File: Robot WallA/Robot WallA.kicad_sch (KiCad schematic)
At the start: 4 parts

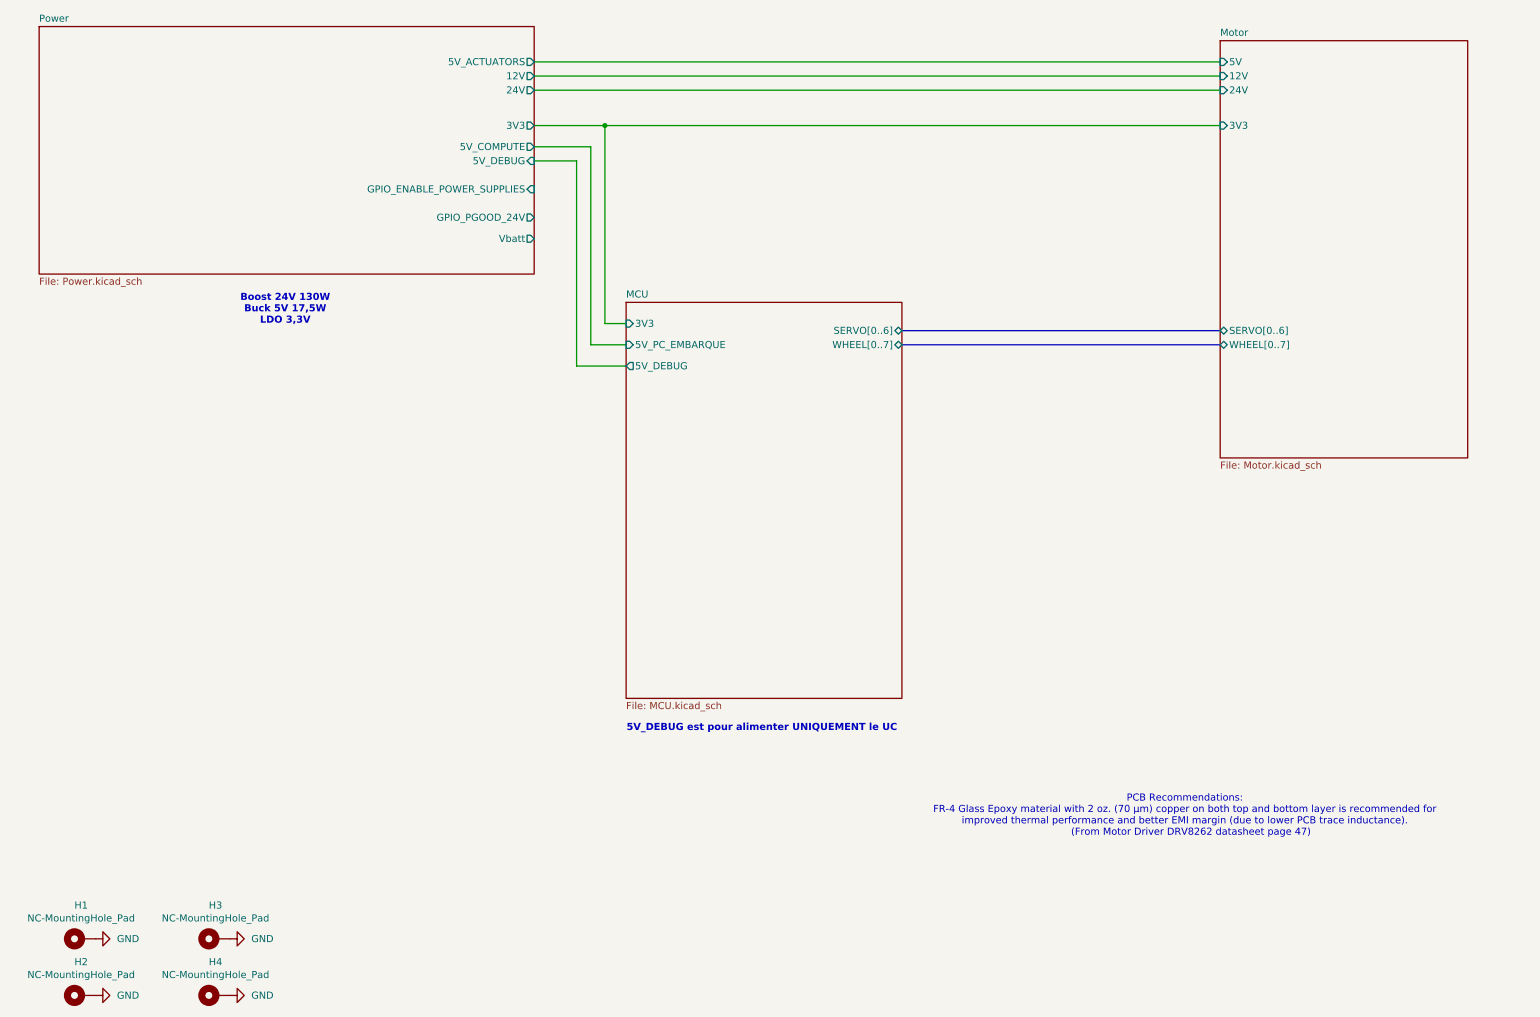
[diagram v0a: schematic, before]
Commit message: Continued to link MCU pins, Added a sheet for servomotors and optional 2 DC motors.
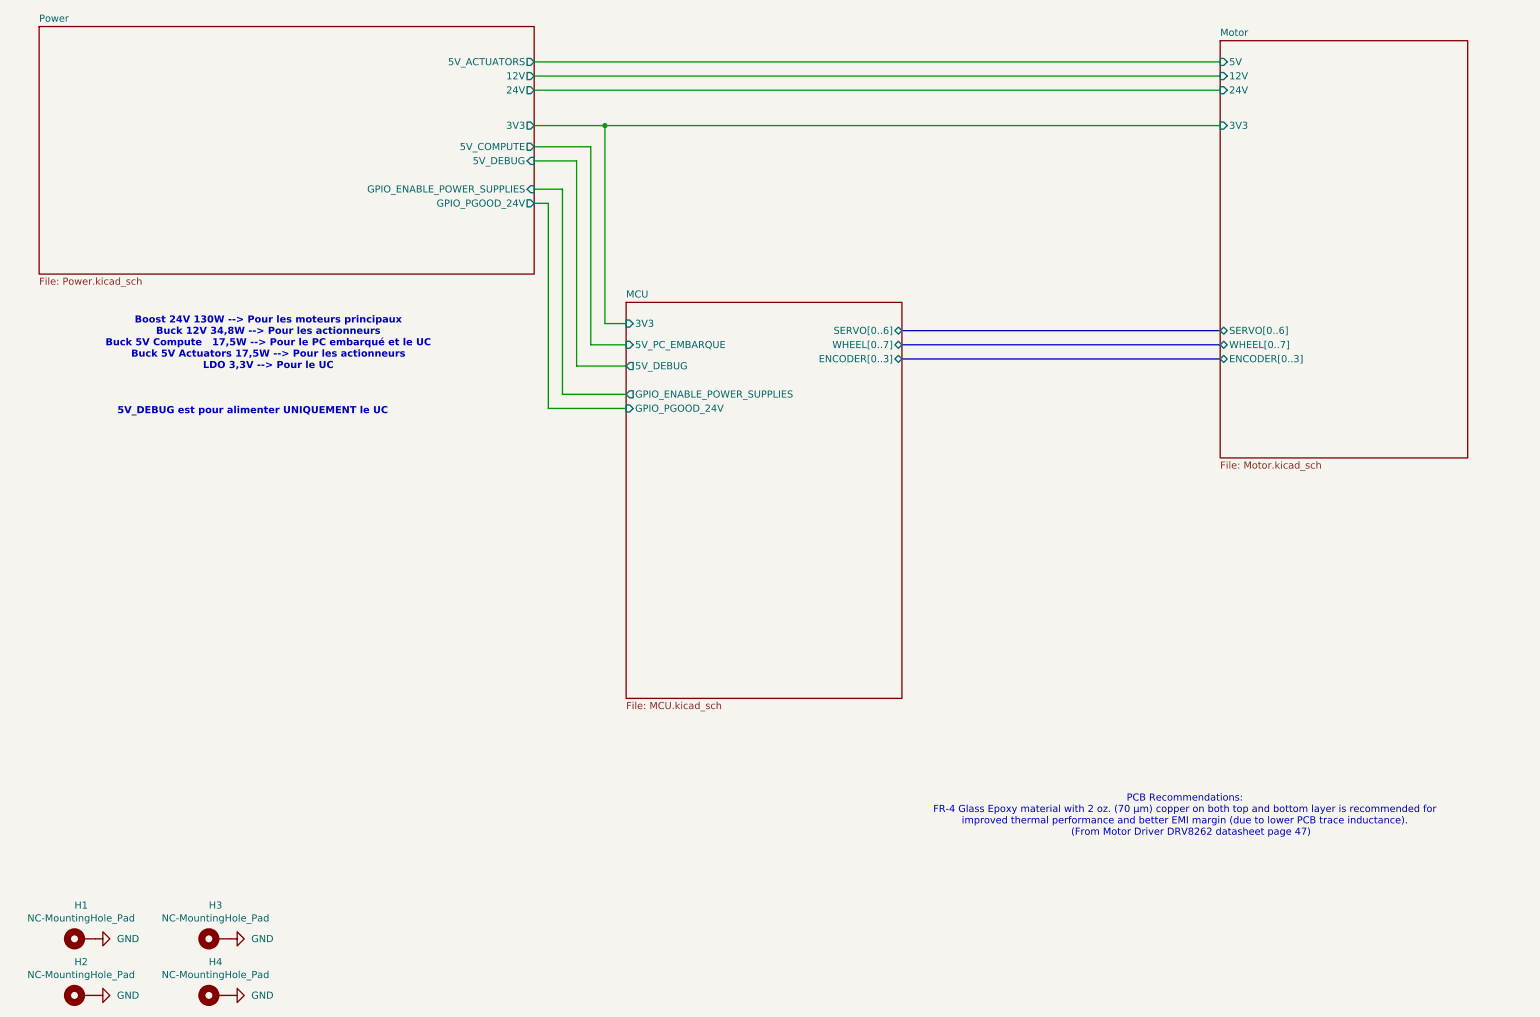
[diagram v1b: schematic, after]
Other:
- sheet MCU ports: added ENCODER[0..3], GPIO_ENABLE_POWER_SUPPLIES, GPIO_PGOOD_24V; removed none
- sheet Motor ports: added ENCODER[0..3]; removed none
- sheet Power ports: added none; removed Vbatt
- note added: "Boost 24V 130W --> Pour les moteurs principaux Buck 12V 34,8W --> Pour les actionneurs Buck 5V Compute 17,5W --> Pour le PC embarqué et le UC Buck 5V Actuators 17,5W --> Pour les actionneurs LDO 3,3V --> Pour le UC"
- note removed: "Boost 24V 130W Buck 5V 17,5W LDO 3,3V"
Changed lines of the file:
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@@
 	(text "5V_DEBUG est pour alimenter UNIQUEMENT le UC"
 		(exclude_from_sim no)
-		(at 150.114 142.494 0)
+		(at 58.674 85.598 0)
 		(effects
 			(font
@@
 		)
 	)
-	(text "Boost 24V 130W\nBuck 5V 17,5W\nLDO 3,3V"
-		(exclude_from_sim no)
-		(at 64.516 67.31 0)
+	(text "Boost 24V 130W --> Pour les moteurs principaux\nBuck 12V 34,8W --> Pour les actionneurs\nBuck 5V Compute   17,5W --> Pour le PC embarqué et le UC\nBuck 5V Actuators 17,5W --> Pour les actionneurs\nLDO 3,3V --> Pour le UC"
+		(exclude_from_sim no)
+		(at 61.468 73.406 0)
 		(effects
 			(font
@@
 	(wire
 		(pts
+			(xy 114.3 82.55) (xy 114.3 45.72)
+		)
+		(stroke
+			(width 0)
+			(type default)
+		)
+	)
+	(wire
+		(pts
 			(xy 109.22 27.94) (xy 232.41 27.94)
 		)
@@
 		)
 	)
+	(bus
+		(pts
+			(xy 175.26 76.2) (xy 232.41 76.2)
+		)
+		(stroke
+			(width 0)
+			(type default)
+		)
+	)
 	(wire
 		(pts
@@
 		)
 	)
+	(wire
+		(pts
+			(xy 109.22 48.26) (xy 111.76 48.26)
+		)
+		(stroke
+			(width 0)
+			(type default)
+		)
+	)
+	(wire
+		(pts
+			(xy 125.73 82.55) (xy 114.3 82.55)
+		)
+		(stroke
+			(width 0)
+			(type default)
+		)
+	)
 	(bus
 		(pts
@@
 	(wire
 		(pts
+			(xy 111.76 85.09) (xy 125.73 85.09)
+		)
+		(stroke
+			(width 0)
+			(type default)
+		)
+	)
+	(wire
+		(pts
 			(xy 119.38 73.66) (xy 125.73 73.66)
 		)
@@
 	(wire
 		(pts
+			(xy 111.76 48.26) (xy 111.76 85.09)
+		)
+		(stroke
+			(width 0)
+			(type default)
+		)
+	)
+	(wire
+		(pts
 			(xy 125.73 77.47) (xy 116.84 77.47)
 		)
@@
 		(pts
 			(xy 109.22 22.86) (xy 232.41 22.86)
+		)
+		(stroke
+			(width 0)
+			(type default)
+		)
+	)
+	(wire
+		(pts
+			(xy 114.3 45.72) (xy 109.22 45.72)
 		)
 		(stroke
@@
 		(dnp no)
 		(fields_autoplaced yes)
-		(property "Reference" "#PWR0113"
+		(property "Reference" "#PWR04"
 			(at 60.96 190.5 0)
 			(effects
@@
 			(project "PCB"
 				(path "/117fd49e-499d-4b54-b58c-f6b538ecca4a"
-					(reference "#PWR0113")
+					(reference "#PWR04")
 					(unit 1)
 				)
@@
 		(dnp no)
 		(fields_autoplaced yes)
-		(property "Reference" "#PWR0112"
+		(property "Reference" "#PWR03"
 			(at 60.96 180.34 0)
 			(effects
@@
 			(project "PCB"
 				(path "/117fd49e-499d-4b54-b58c-f6b538ecca4a"
-					(reference "#PWR0112")
+					(reference "#PWR03")
 					(unit 1)
 				)
@@
 		(dnp no)
 		(fields_autoplaced yes)
-		(property "Reference" "#PWR0110"
+		(property "Reference" "#PWR01"
 			(at 36.83 180.34 0)
 			(effects
@@
 			(project ""
 				(path "/117fd49e-499d-4b54-b58c-f6b538ecca4a"
-					(reference "#PWR0110")
+					(reference "#PWR01")
 					(unit 1)
 				)
@@
 		(dnp no)
 		(fields_autoplaced yes)
-		(property "Reference" "#PWR0111"
+		(property "Reference" "#PWR02"
 			(at 36.83 190.5 0)
 			(effects
@@
 			(project "PCB"
 				(path "/117fd49e-499d-4b54-b58c-f6b538ecca4a"
-					(reference "#PWR0111")
+					(reference "#PWR02")
 					(unit 1)
 				)
@@
 			)
 		)
+		(pin "ENCODER[0..3]" bidirectional
+			(at 232.41 76.2 180)
+			(effects
+				(font
+					(size 1.27 1.27)
+				)
+				(justify left)
+			)
+		)
 		(instances
-			(project "PCB"
+			(project "Robot WallA"
 				(path "/117fd49e-499d-4b54-b58c-f6b538ecca4a"
 					(page "3")
@@
 			)
 		)
+		(pin "ENCODER[0..3]" bidirectional
+			(at 175.26 76.2 0)
+			(effects
+				(font
+					(size 1.27 1.27)
+				)
+				(justify right)
+			)
+		)
+		(pin "GPIO_ENABLE_POWER_SUPPLIES" output
+			(at 125.73 82.55 180)
+			(effects
+				(font
+					(size 1.27 1.27)
+				)
+				(justify left)
+			)
+		)
+		(pin "GPIO_PGOOD_24V" input
+			(at 125.73 85.09 180)
+			(effects
+				(font
+					(size 1.27 1.27)
+				)
+				(justify left)
+			)
+		)
 		(instances
-			(project "PCB"
+			(project "Robot WallA"
 				(path "/117fd49e-499d-4b54-b58c-f6b538ecca4a"
 					(page "2")
@@
 		)
 		(pin "GPIO_PGOOD_24V" output
-			(at 109.22 50.8 0)
-			(effects
-				(font
-					(size 1.27 1.27)
-				)
-				(justify right)
-			)
-		)
-		(pin "Vbatt" output
-			(at 109.22 54.61 0)
+			(at 109.22 48.26 0)
 			(effects
 				(font
@@
 		)
 		(instances
-			(project "PCB"
+			(project "Robot WallA"
 				(path "/117fd49e-499d-4b54-b58c-f6b538ecca4a"
 					(page "5")

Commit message: Defined every footprints
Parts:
- H1, H4: value NC-MountingHole_Pad -> MountingHole_Pad; Manufacturer_Part_Number NC -> (none); Mouser Reference NC -> (none); RS Reference NC -> (none)
- H2: renamed from H3; value NC-MountingHole_Pad -> MountingHole_Pad; Manufacturer_Part_Number NC -> (none); Mouser Reference NC -> (none); RS Reference NC -> (none)
- H3: renamed from H2; value NC-MountingHole_Pad -> MountingHole_Pad; Manufacturer_Part_Number NC -> (none); Mouser Reference NC -> (none); RS Reference NC -> (none)
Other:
- added sheet DistanceMeter (DistanceMeter.kicad_sch)
- sheet MCU ports: added SECONDARY_MOTOR[0..7]; removed none
- sheet Motor ports: added SECONDARY_MOTOR[0..7]; removed none
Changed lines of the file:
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@@
+		)
+	)
+	(bus
+		(pts
+			(xy 175.26 78.74) (xy 232.41 78.74)
+		)
+		(stroke
+			(width 0)
+			(type default)
 		)
 	)
@@
 			)
 		)
-		(property "Value" "NC-MountingHole_Pad"
+		(property "Value" "MountingHole_Pad"
 			(at 27.8638 176.6316 90)
 			(effects
@@
 			)
 		)
-		(property "Manufacturer_Part_Number" "NC"
-			(at 27.94 180.34 0)
-			(effects
-				(font
-					(size 1.27 1.27)
-				)
-				(hide yes)
-			)
-		)
-		(property "Mouser Reference" "NC"
-			(at 27.94 180.34 0)
-			(effects
-				(font
-					(size 1.27 1.27)
-				)
-				(hide yes)
-			)
-		)
-		(property "RS Reference" "NC"
+		(property "Manufacturer_Part_Number" ""
 			(at 27.94 180.34 0)
 			(effects
@@
 		(dnp no)
 		(fields_autoplaced yes)
-		(property "Reference" "#PWR03"
+		(property "Reference" "#PWR02"
 			(at 60.96 180.34 0)
 			(effects
@@
 			(project "PCB"
 				(path "/117fd49e-499d-4b54-b58c-f6b538ecca4a"
-					(reference "#PWR03")
+					(reference "#PWR02")
 					(unit 1)
 				)
@@
 		(dnp no)
 		(fields_autoplaced yes)
-		(property "Reference" "#PWR02"
+		(property "Reference" "#PWR03"
 			(at 36.83 190.5 0)
 			(effects
@@
 			(project "PCB"
 				(path "/117fd49e-499d-4b54-b58c-f6b538ecca4a"
-					(reference "#PWR02")
+					(reference "#PWR03")
 					(unit 1)
 				)
@@
 		(on_board yes)
 		(dnp no)
-		(property "Reference" "H2"
+		(property "Reference" "H3"
 			(at 27.8638 184.4802 90)
 			(effects
@@
 			)
 		)
-		(property "Value" "NC-MountingHole_Pad"
+		(property "Value" "MountingHole_Pad"
 			(at 27.8638 186.7916 90)
 			(effects
@@
 			)
 		)
-		(property "Manufacturer_Part_Number" "NC"
+		(property "Manufacturer_Part_Number" ""
 			(at 27.94 190.5 0)
 			(effects
@@
 			)
 		)
-		(property "Mouser Reference" "NC"
-			(at 27.94 190.5 0)
-			(effects
-				(font
-					(size 1.27 1.27)
-				)
-				(hide yes)
-			)
-		)
-		(property "RS Reference" "NC"
-			(at 27.94 190.5 0)
-			(effects
-				(font
-					(size 1.27 1.27)
-				)
-				(hide yes)
-			)
-		)
 		(pin "1"
 		)
@@
 			(project "PCB"
 				(path "/117fd49e-499d-4b54-b58c-f6b538ecca4a"
-					(reference "H2")
+					(reference "H3")
 					(unit 1)
 				)
@@
 		(on_board yes)
 		(dnp no)
-		(property "Reference" "H3"
+		(property "Reference" "H2"
 			(at 51.9938 174.3202 90)
 			(effects
@@
 			)
 		)
-		(property "Value" "NC-MountingHole_Pad"
+		(property "Value" "MountingHole_Pad"
 			(at 51.9938 176.6316 90)
 			(effects
@@
 			)
 		)
-		(property "Manufacturer_Part_Number" "NC"
+		(property "Manufacturer_Part_Number" ""
 			(at 52.07 180.34 0)
 			(effects
@@
 			)
 		)
-		(property "Mouser Reference" "NC"
-			(at 52.07 180.34 0)
-			(effects
-				(font
-					(size 1.27 1.27)
-				)
-				(hide yes)
-			)
-		)
-		(property "RS Reference" "NC"
-			(at 52.07 180.34 0)
-			(effects
-				(font
-					(size 1.27 1.27)
-				)
-				(hide yes)
-			)
-		)
 		(pin "1"
 		)
@@
 			(project "PCB"
 				(path "/117fd49e-499d-4b54-b58c-f6b538ecca4a"
-					(reference "H3")
+					(reference "H2")
 					(unit 1)
 				)
@@
 			)
 		)
-		(property "Value" "NC-MountingHole_Pad"
+		(property "Value" "MountingHole_Pad"
 			(at 51.9938 186.7916 90)
 			(effects
@@
 			)
 		)
-		(property "Manufacturer_Part_Number" "NC"
-			(at 52.07 190.5 0)
-			(effects
-				(font
-					(size 1.27 1.27)
-				)
-				(hide yes)
-			)
-		)
-		(property "Mouser Reference" "NC"
-			(at 52.07 190.5 0)
-			(effects
-				(font
-					(size 1.27 1.27)
-				)
-				(hide yes)
-			)
-		)
-		(property "RS Reference" "NC"
+		(property "Manufacturer_Part_Number" ""
 			(at 52.07 190.5 0)
 			(effects
@@
 					(reference "H4")
 					(unit 1)
+				)
+			)
+		)
+	)
+	(sheet
+		(at 213.36 107.95)
+		(size 60.96 36.83)
+		(exclude_from_sim no)
+		(in_bom yes)
+		(on_board yes)
+		(dnp no)
+		(fields_autoplaced yes)
+		(stroke
+			(width 0.1524)
+			(type solid)
+		)
+		(fill
+			(color 0 0 0 0.0000)
+		)
+		(property "Sheetname" "DistanceMeter"
+			(at 213.36 107.2384 0)
+			(effects
+				(font
+					(size 1.27 1.27)
+				)
+				(justify left bottom)
+			)
+		)
+		(property "Sheetfile" "DistanceMeter.kicad_sch"
+			(at 213.36 145.3646 0)
+			(effects
+				(font
+					(size 1.27 1.27)
+				)
+				(justify left top)
+			)
+		)
+		(instances
+			(project "Robot WallA"
+				(path "/117fd49e-499d-4b54-b58c-f6b538ecca4a"
+					(page "17")
 				)
 			)
@@
 			)
 		)
+		(pin "SECONDARY_MOTOR[0..7]" bidirectional
+			(at 232.41 78.74 180)
+			(effects
+				(font
+					(size 1.27 1.27)
+				)
+				(justify left)
+			)
+		)
 		(instances
 			(project "Robot WallA"
 				(path "/117fd49e-499d-4b54-b58c-f6b538ecca4a"
-					(page "3")
+					(page "13")
 				)
 			)
@@
 			)
 		)
+		(pin "SECONDARY_MOTOR[0..7]" bidirectional
+			(at 175.26 78.74 0)
+			(effects
+				(font
+					(size 1.27 1.27)
+				)
+				(justify right)
+			)
+		)
 		(instances
 			(project "Robot WallA"
@@
 			(project "Robot WallA"
 				(path "/117fd49e-499d-4b54-b58c-f6b538ecca4a"
-					(page "5")
-				)
-			)
+					(page "8")
+				)
+			)

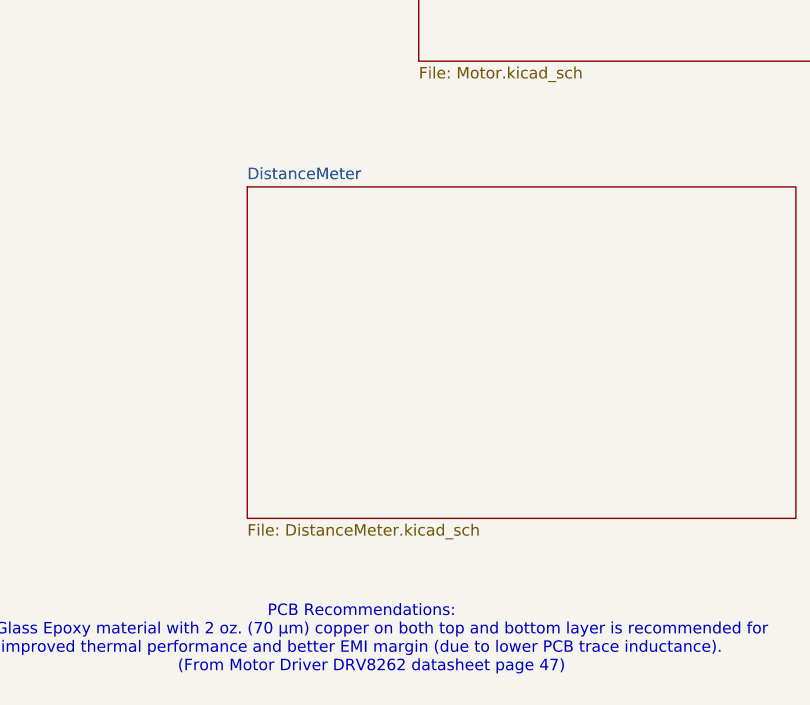
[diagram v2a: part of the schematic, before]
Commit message: Created sensors sheet (for distance meters and others)
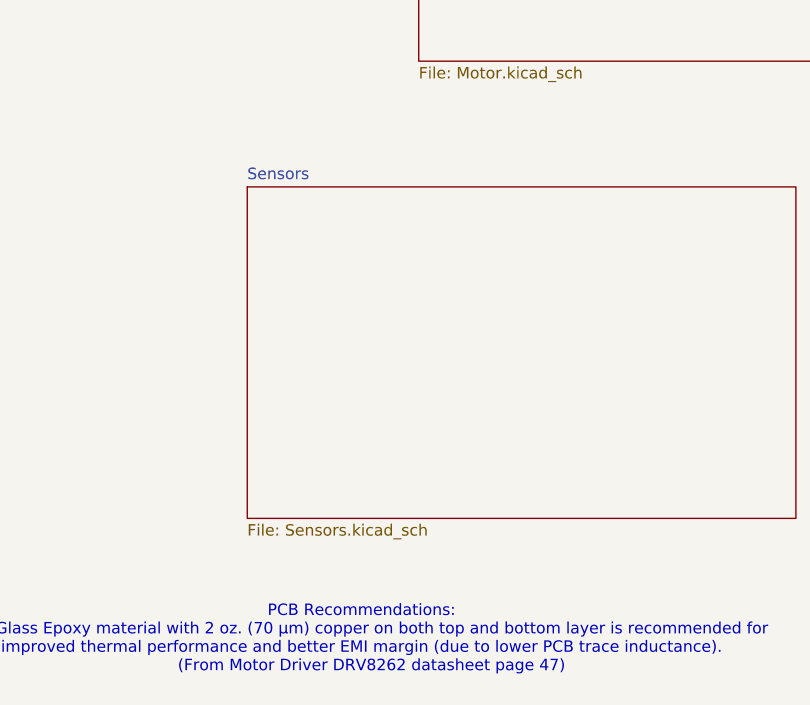
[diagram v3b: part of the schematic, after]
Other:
- sheet DistanceMeter renamed Sensors
- sheet Sensors: file DistanceMeter.kicad_sch -> Sensors.kicad_sch
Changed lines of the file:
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@@
 			(color 0 0 0 0.0000)
 		)
-		(property "Sheetname" "DistanceMeter"
+		(property "Sheetname" "Sensors"
 			(at 213.36 107.2384 0)
 			(effects
@@
 			)
 		)
-		(property "Sheetfile" "DistanceMeter.kicad_sch"
+		(property "Sheetfile" "Sensors.kicad_sch"
 			(at 213.36 145.3646 0)
 			(effects

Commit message: Startes to write README
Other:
- note added: "Boost 24V 130W --> Pour les moteurs principaux Buck 12V 69,6W --> Pour les actionneurs Buck 5V Compute 17,5W --> Pour le PC embarqué et le UC Buck 5V Actuators 17,5W --> Pour les actionneurs LDO 3,3V --> Pour le UC"
- note removed: "Boost 24V 130W --> Pour les moteurs principaux Buck 12V 34,8W --> Pour les actionneurs Buck 5V Compute 17,5W --> Pour le PC embarqué et le UC Buck 5V Actuators 17,5W --> Pour les actionneurs LDO 3,3V --> Pour le UC"
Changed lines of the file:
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@@
 		)
 	)
-	(text "Boost 24V 130W --> Pour les moteurs principaux\nBuck 12V 34,8W --> Pour les actionneurs\nBuck 5V Compute   17,5W --> Pour le PC embarqué et le UC\nBuck 5V Actuators 17,5W --> Pour les actionneurs\nLDO 3,3V --> Pour le UC"
+	(text "Boost 24V 130W --> Pour les moteurs principaux\nBuck 12V 69,6W --> Pour les actionneurs\nBuck 5V Compute   17,5W --> Pour le PC embarqué et le UC\nBuck 5V Actuators 17,5W --> Pour les actionneurs\nLDO 3,3V --> Pour le UC"
 		(exclude_from_sim no)
 		(at 61.468 73.406 0)
